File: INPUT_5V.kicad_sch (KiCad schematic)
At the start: 5 parts

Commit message: improved analogs
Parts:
- R15: renamed from R43; value 10k -> 1k
- R25: renamed from R44; value 1k -> 1.5k
- renumbered C56 to C48, D10 to D1, R42 to R14
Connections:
- net GND renamed AGND
- net INPUT renamed RAW
- net OUTPUT renamed IO

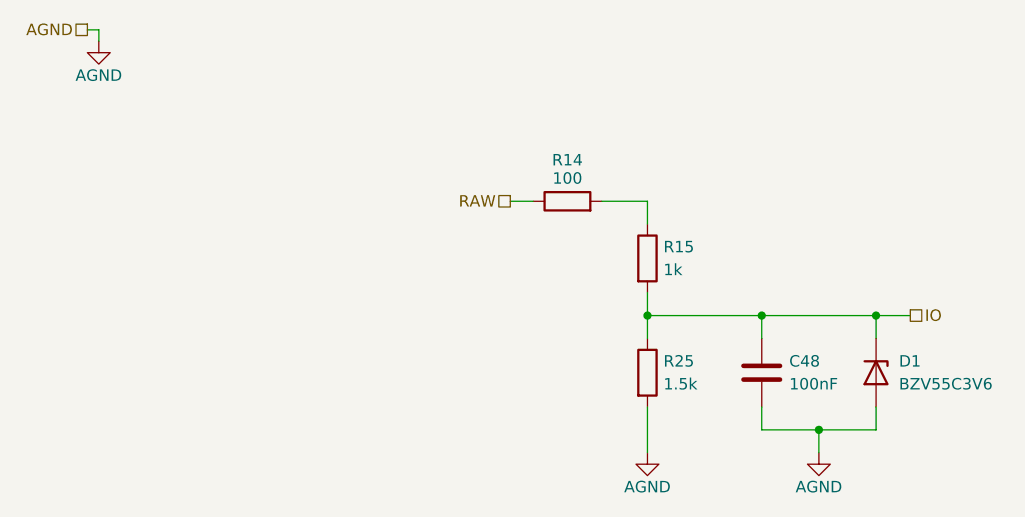
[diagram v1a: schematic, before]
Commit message: redid annotations, added test point
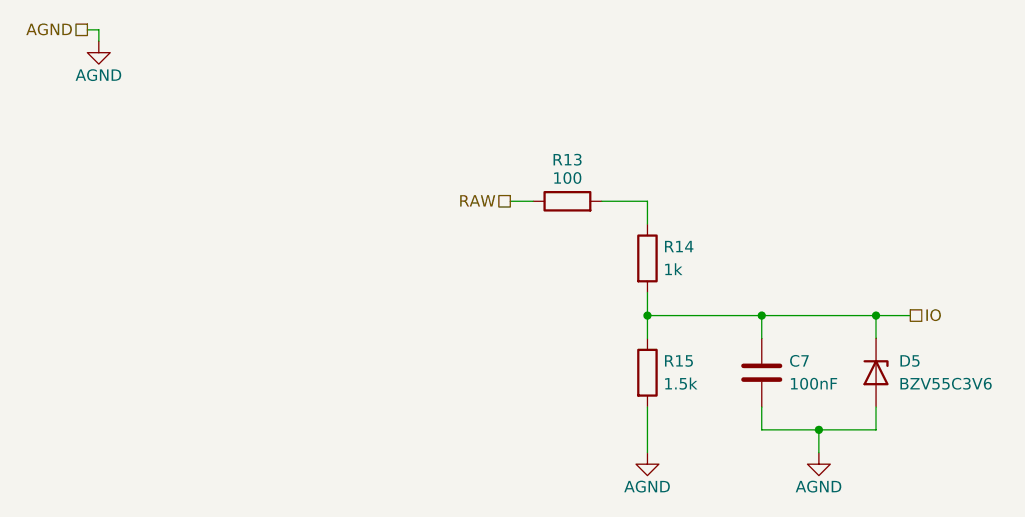
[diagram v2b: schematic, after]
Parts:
- renumbered C48 to C7, D1 to D5, R14 to R13, R15 to R14, R25 to R15
